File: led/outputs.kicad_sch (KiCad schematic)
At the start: 14 parts, among them J1 TBL002A-350-08GR-2OR, K1 G6DN-1A_DC4.5, K2 G6DN-1A_DC4.5, K3 G6DN-1A_DC4.5, Q5 BS170, Q6 BS170, Q7 BS170

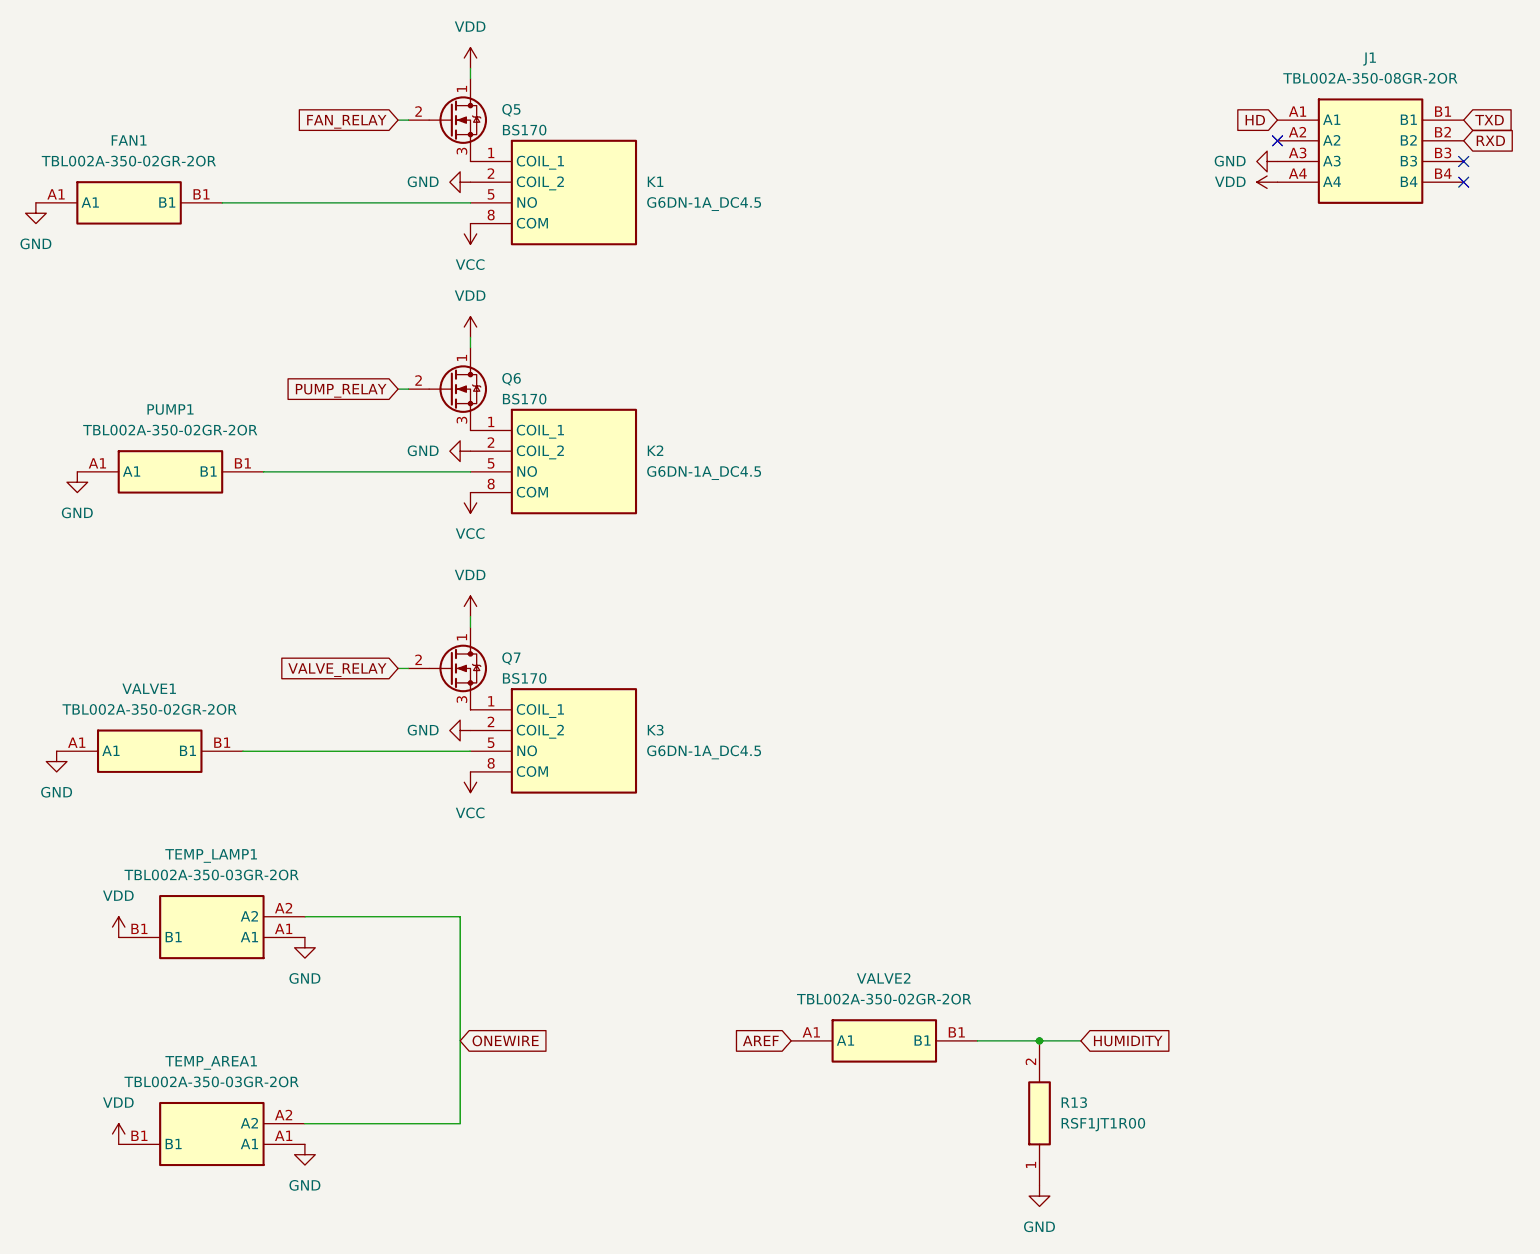
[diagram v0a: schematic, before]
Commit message: using single and dual top switch current driver circuits
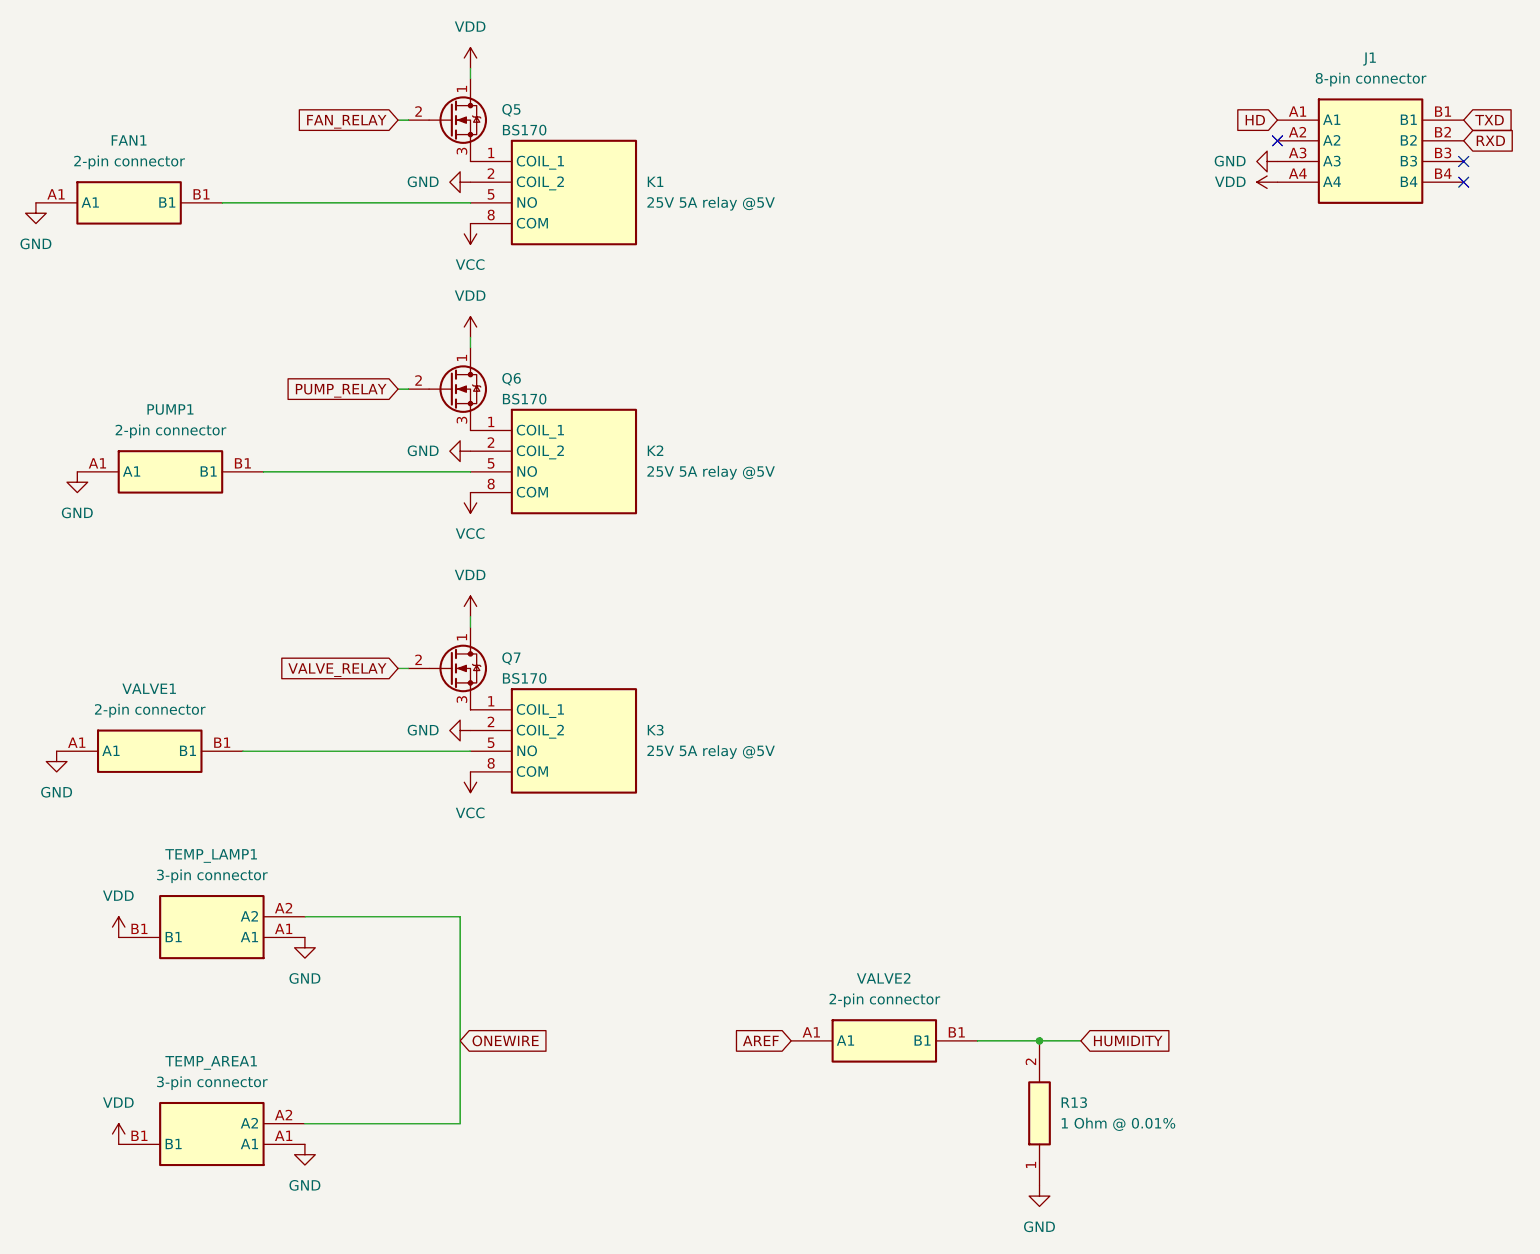
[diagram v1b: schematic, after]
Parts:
- FAN1, PUMP1, VALVE1, VALVE2: value TBL002A-350-02GR-2OR -> 2-pin connector
- J1: value TBL002A-350-08GR-2OR -> 8-pin connector
- K1, K2, K3: value G6DN-1A_DC4.5 -> 25V 5A relay @5V; footprint arduino-library:G6DN1ADC45 -> arduino-library:G6DN-1A-L; Mouser Part Number 653-G6DN1ADC45 -> 653-G6DN1ADC5
- Q5, Q6, Q7: Mouser Part Number (none) -> 512-BS170
- R13: value RSF1JT1R00 -> 1 Ohm @ 0.01%; Mouser Part Number (none) -> 708-RSF1JT1R00
- TEMP_AREA1, TEMP_LAMP1: value TBL002A-350-03GR-2OR -> 3-pin connector
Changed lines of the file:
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@@
+			)
+		)
+		(property "Mouser Part Number" "512-BS170"
+			(at 72.39 105.41 0)
+			(effects
+				(font
+					(size 1.27 1.27)
+				)
+				(hide yes)
 			)
 		)
@@
 			)
 		)
-		(property "Value" "G6DN-1A_DC4.5"
+		(property "Value" "25V 5A relay @5V"
 			(at 96.52 81.2799 0)
 			(effects
@@
 			)
 		)
-		(property "Footprint" "arduino-library:G6DN1ADC45"
+		(property "Footprint" "arduino-library:G6DN-1A-L"
 			(at 96.52 171.12 0)
 			(effects
@@
 			)
 		)
-		(property "Datasheet" "https://componentsearchengine.com/Datasheets/1/G6DN-1A DC4.5.pdf"
+		(property "Datasheet" "https://omronfs.omron.com/en_US/ecb/products/pdf/en-g6dn.pdf"
 			(at 96.52 271.12 0)
 			(effects
@@
 			)
 		)
-		(property "Mouser Part Number" "653-G6DN1ADC45"
+		(property "Mouser Part Number" "653-G6DN1ADC5"
 			(at 96.52 571.12 0)
 			(effects
@@
 			)
 		)
-		(property "Value" "TBL002A-350-02GR-2OR"
+		(property "Value" "2-pin connector"
 			(at 125.73 146.05 0)
 			(effects
@@
 			)
 		)
-		(property "Value" "G6DN-1A_DC4.5"
+		(property "Value" "25V 5A relay @5V"
 			(at 96.52 115.5699 0)
 			(effects
@@
 			)
 		)
-		(property "Footprint" "arduino-library:G6DN1ADC45"
+		(property "Footprint" "arduino-library:G6DN-1A-L"
 			(at 96.52 205.41 0)
 			(effects
@@
 			)
 		)
-		(property "Datasheet" "https://componentsearchengine.com/Datasheets/1/G6DN-1A DC4.5.pdf"
+		(property "Datasheet" "https://omronfs.omron.com/en_US/ecb/products/pdf/en-g6dn.pdf"
 			(at 96.52 305.41 0)
 			(effects
@@
 			)
 		)
-		(property "Mouser Part Number" "653-G6DN1ADC45"
+		(property "Mouser Part Number" "653-G6DN1ADC5"
 			(at 96.52 605.41 0)
 			(effects
@@
 			)
 		)
+		(property "Mouser Part Number" "512-BS170"
+			(at 72.39 38.1 0)
+			(effects
+				(font
+					(size 1.27 1.27)
+				)
+				(hide yes)
+			)
+		)
 		(pin "3"
 		)
@@
 			)
 		)
-		(property "Value" "TBL002A-350-02GR-2OR"
+		(property "Value" "2-pin connector"
 			(at 33.02 43.18 0)
 			(effects
@@
 			)
 		)
-		(property "Value" "G6DN-1A_DC4.5"
+		(property "Value" "25V 5A relay @5V"
 			(at 96.52 48.2599 0)
 			(effects
@@
 			)
 		)
-		(property "Footprint" "arduino-library:G6DN1ADC45"
+		(property "Footprint" "arduino-library:G6DN-1A-L"
 			(at 96.52 138.1 0)
 			(effects
@@
 			)
 		)
-		(property "Datasheet" "https://componentsearchengine.com/Datasheets/1/G6DN-1A DC4.5.pdf"
+		(property "Datasheet" "https://omronfs.omron.com/en_US/ecb/products/pdf/en-g6dn.pdf"
 			(at 96.52 238.1 0)
 			(effects
@@
 			)
 		)
-		(property "Mouser Part Number" "653-G6DN1ADC45"
+		(property "Mouser Part Number" "653-G6DN1ADC5"
 			(at 96.52 538.1 0)
 			(effects
@@
 			)
 		)
-		(property "Value" "TBL002A-350-03GR-2OR"
+		(property "Value" "3-pin connector"
 			(at 43.18 156.21 0)
 			(effects
@@
 			)
 		)
-		(property "Value" "TBL002A-350-08GR-2OR"
+		(property "Value" "8-pin connector"
 			(at 185.42 33.02 0)
 			(effects
@@
 			)
 		)
-		(property "Value" "RSF1JT1R00"
+		(property "Value" "1 Ohm @ 0.01%"
 			(at 147.32 161.2899 90)
 			(effects
@@
 			)
 		)
-		(property "Mouser Part Number" ""
+		(property "Mouser Part Number" "708-RSF1JT1R00"
 			(at 640.97 154.94 0)
 			(effects
@@
 			)
 		)
-		(property "Value" "TBL002A-350-02GR-2OR"
+		(property "Value" "2-pin connector"
 			(at 35.56 110.49 0)
 			(effects
@@
 			)
 		)
-		(property "Value" "TBL002A-350-02GR-2OR"
+		(property "Value" "2-pin connector"
 			(at 38.1 76.2 0)
 			(effects
@@
 			)
 		)
+		(property "Mouser Part Number" "512-BS170"
+			(at 72.39 71.12 0)
+			(effects
+				(font
+					(size 1.27 1.27)
+				)
+				(hide yes)
+			)
+		)
 		(pin "3"
 		)
@@
 			)
 		)
-		(property "Value" "TBL002A-350-03GR-2OR"
+		(property "Value" "3-pin connector"
 			(at 43.18 130.81 0)
 			(effects
